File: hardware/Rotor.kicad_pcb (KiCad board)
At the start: 2 copper layers, 200 x 200 mm, 0 parts

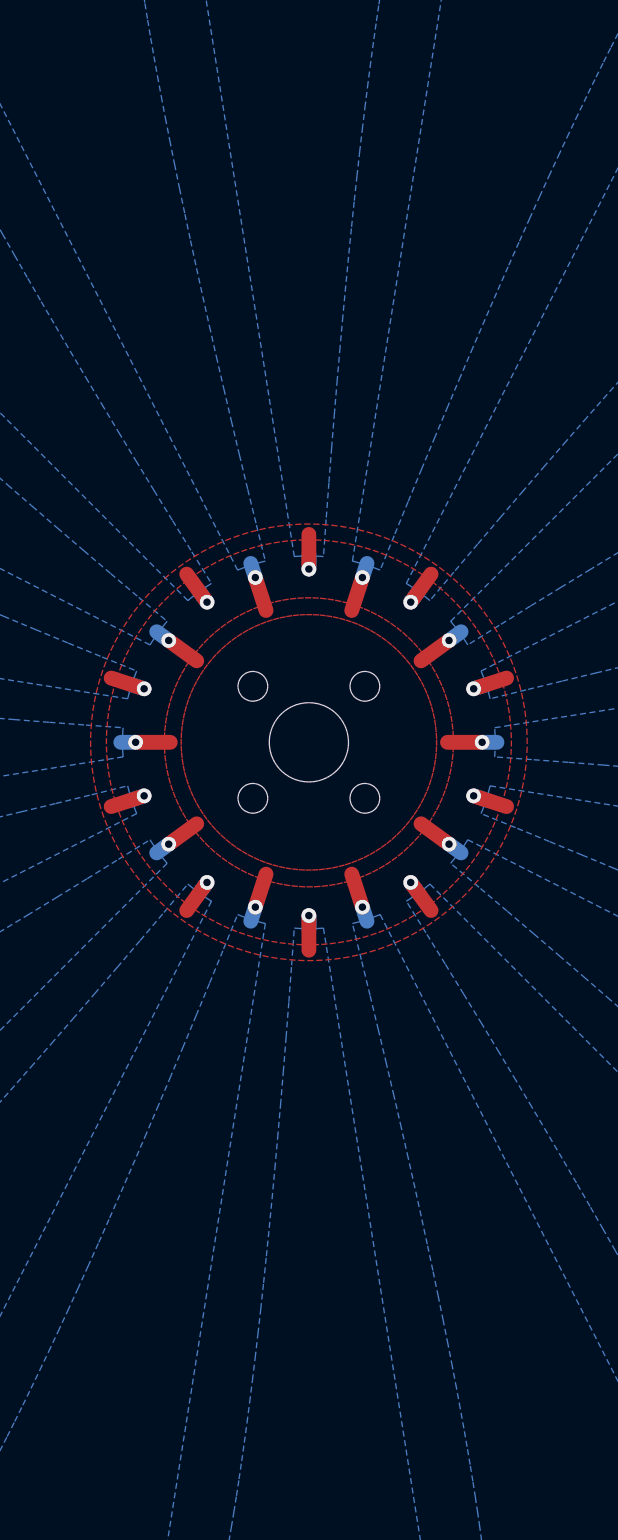
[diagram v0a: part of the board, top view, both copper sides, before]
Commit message: Libraries and generator design
Updated the generator design.
Added a libraries folder.
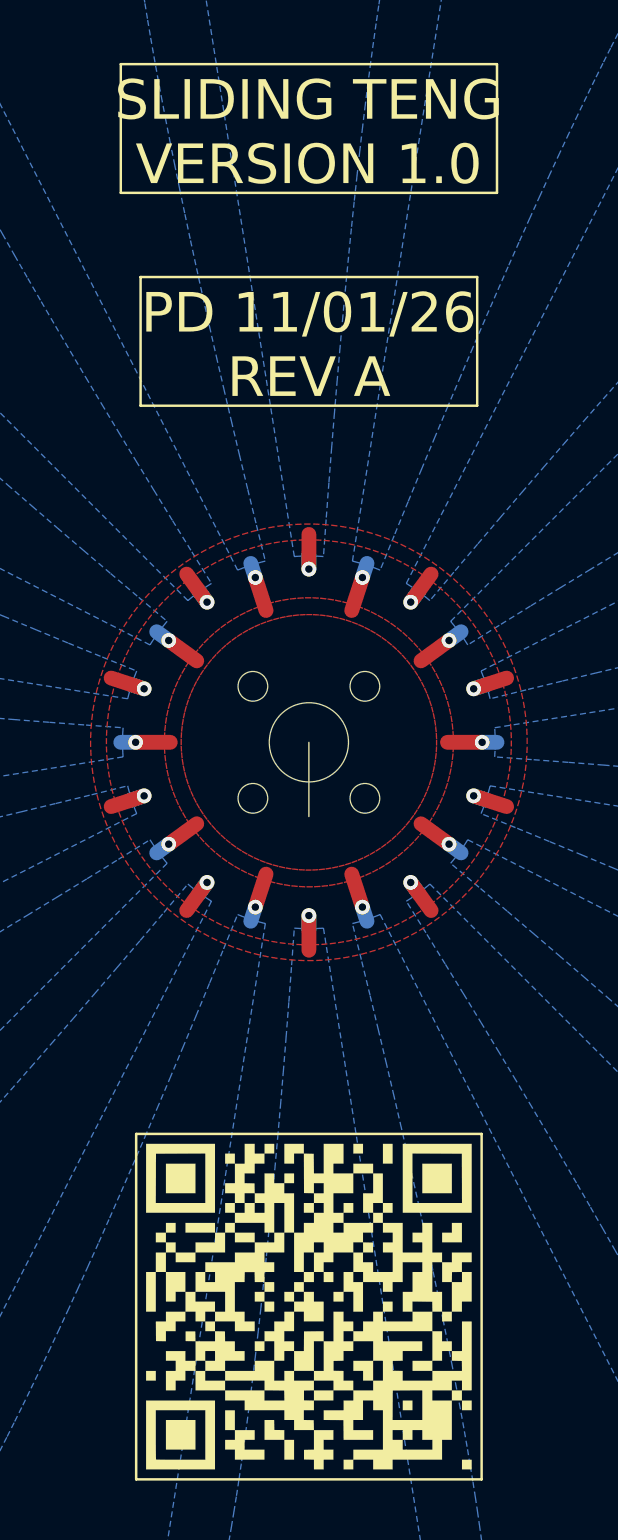
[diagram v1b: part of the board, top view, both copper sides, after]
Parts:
- added G***: LOGO, TENG:QR, F.Cu at (200.0, 207.0)
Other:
- board text added: "PD 11/01/26"
- board text added: "REV A"
- board text added: "SLIDING TENG"
- board text added: "VERSION 1.0"

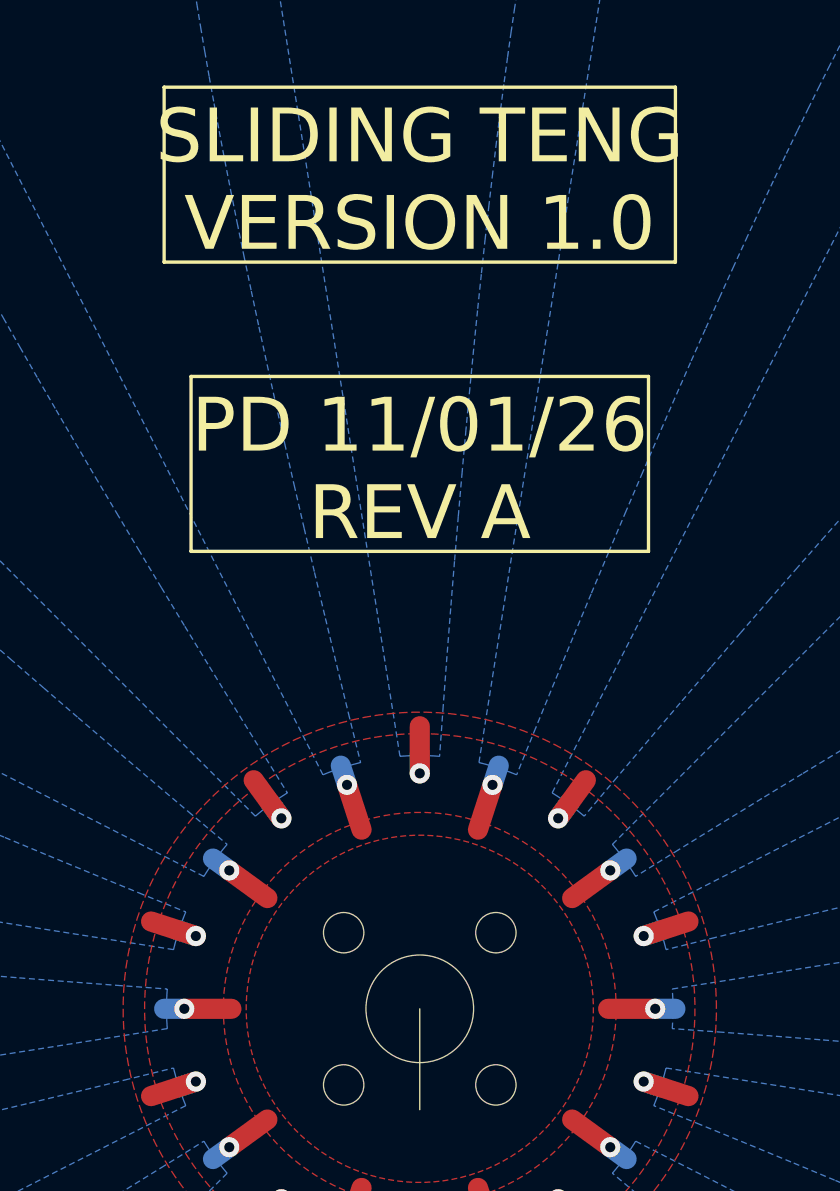
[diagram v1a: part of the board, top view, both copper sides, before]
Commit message: Generator design
Updated the rotor board design.
Updated the stator board design.
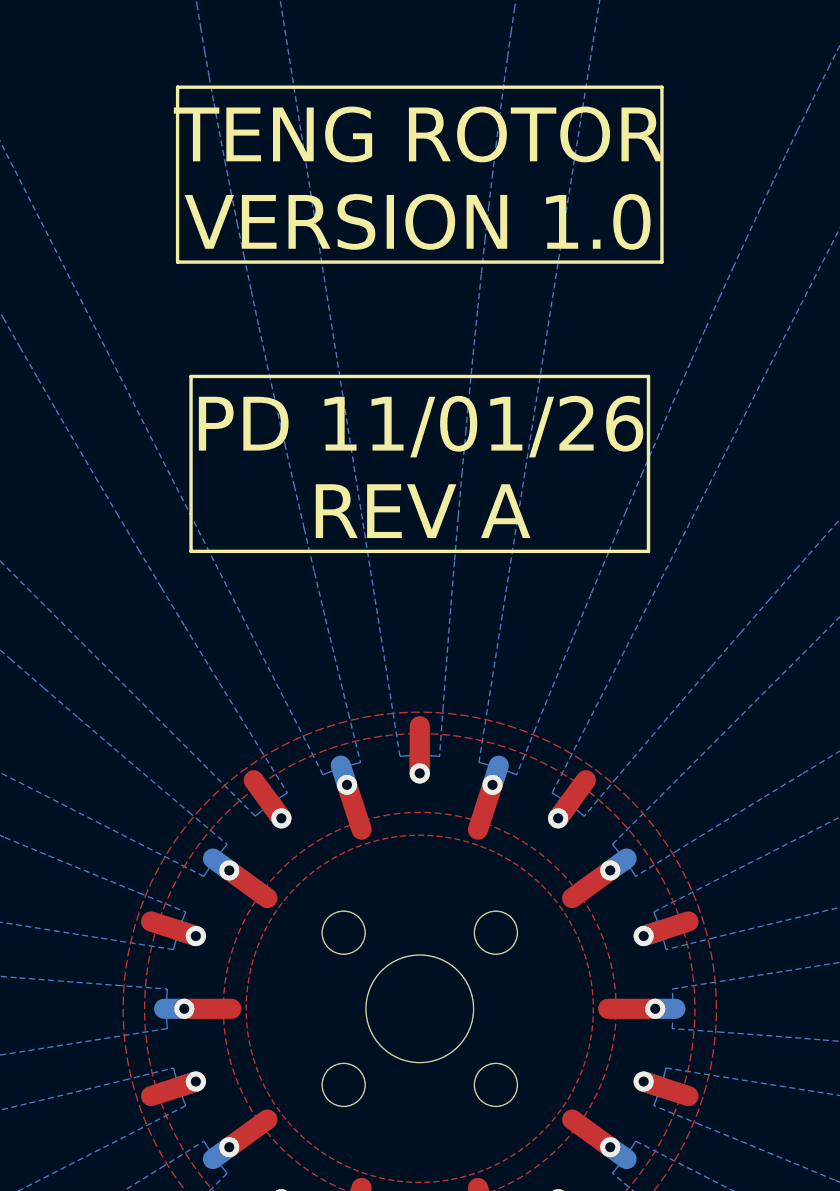
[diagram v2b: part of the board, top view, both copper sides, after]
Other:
- outline, holes or cut-outs redrawn
- board text added: "TENG ROTOR"
- board text removed: "SLIDING TENG"

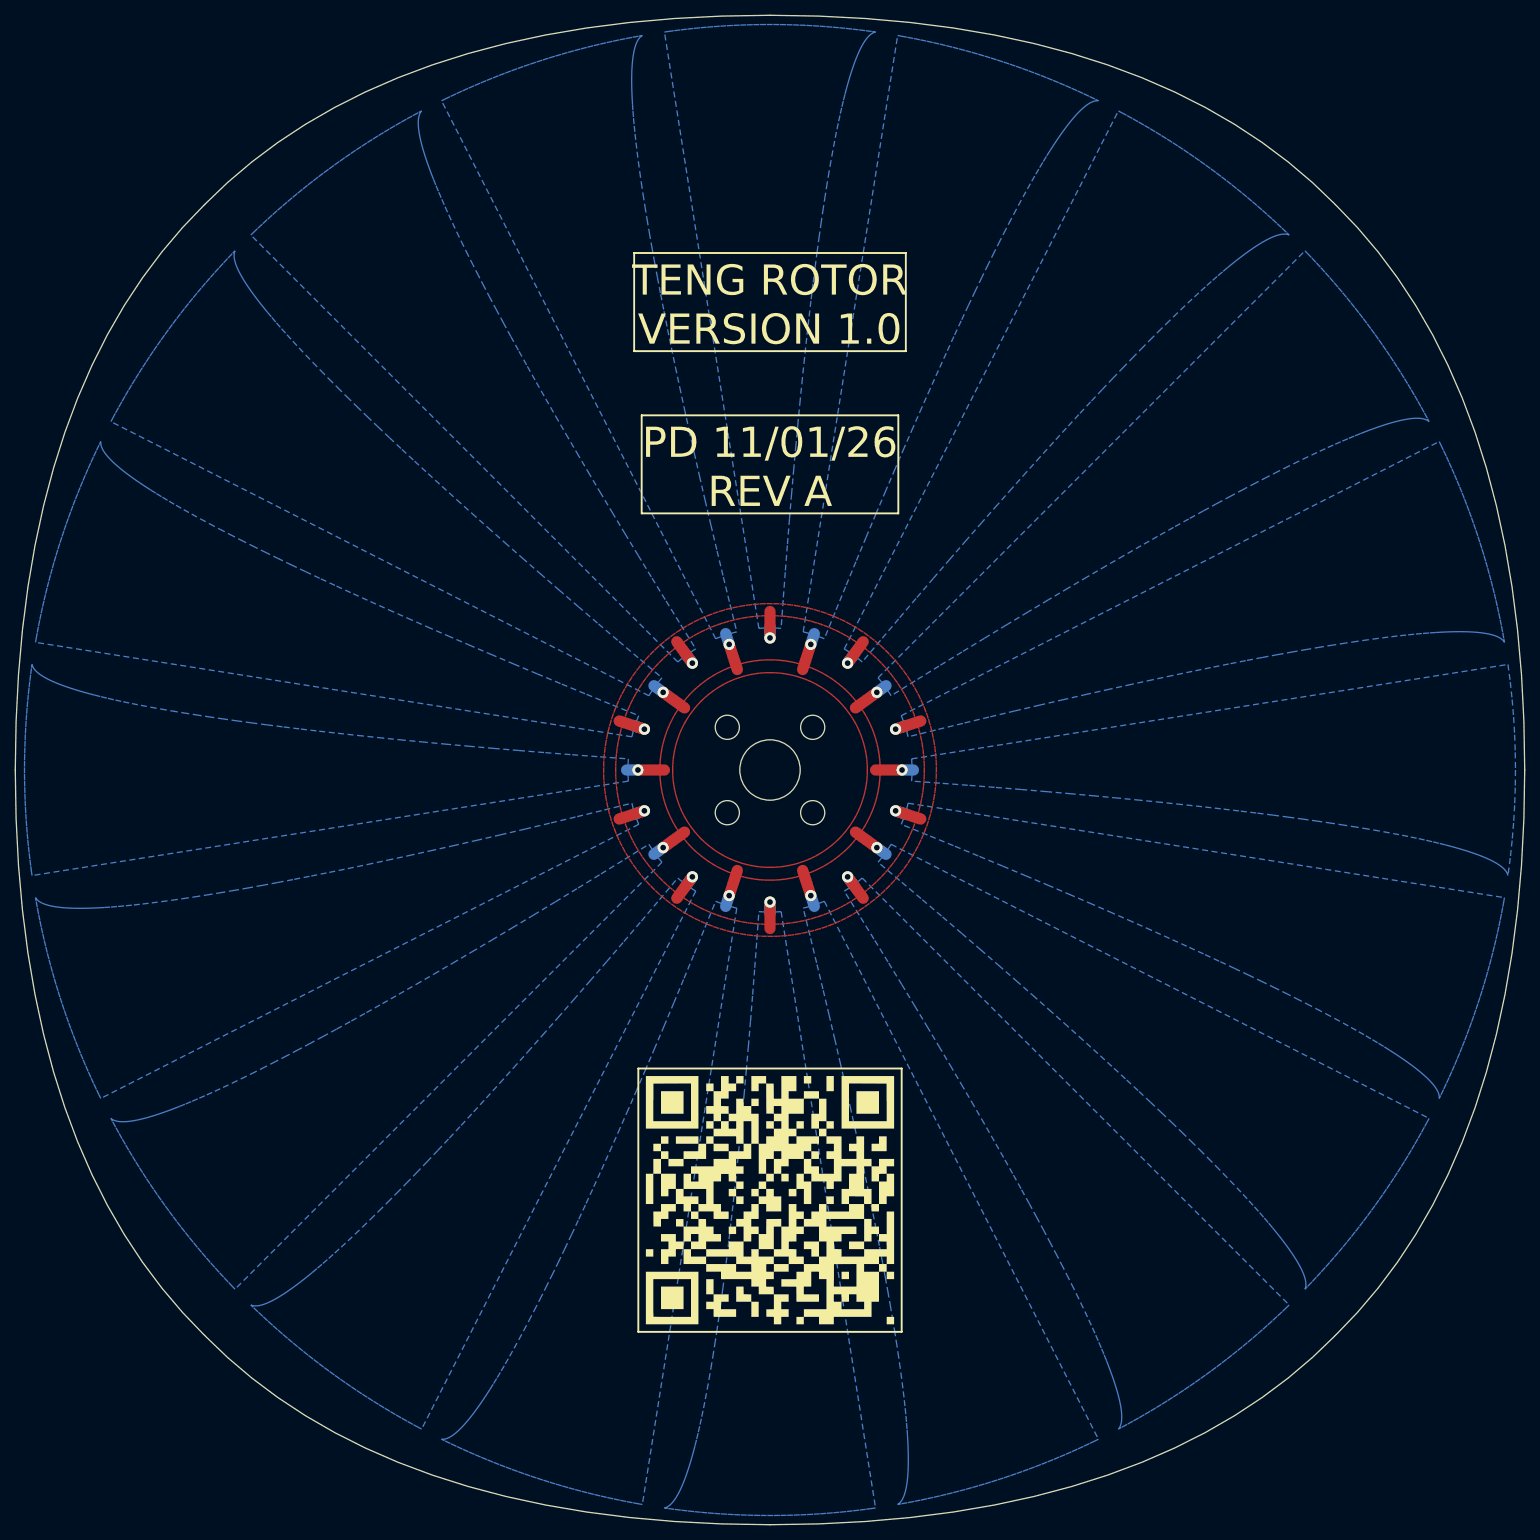
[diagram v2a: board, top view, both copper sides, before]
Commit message: Project update
Updated the project to work with KiCad 10.0.
Updated the exposed pad areas for both layouts.
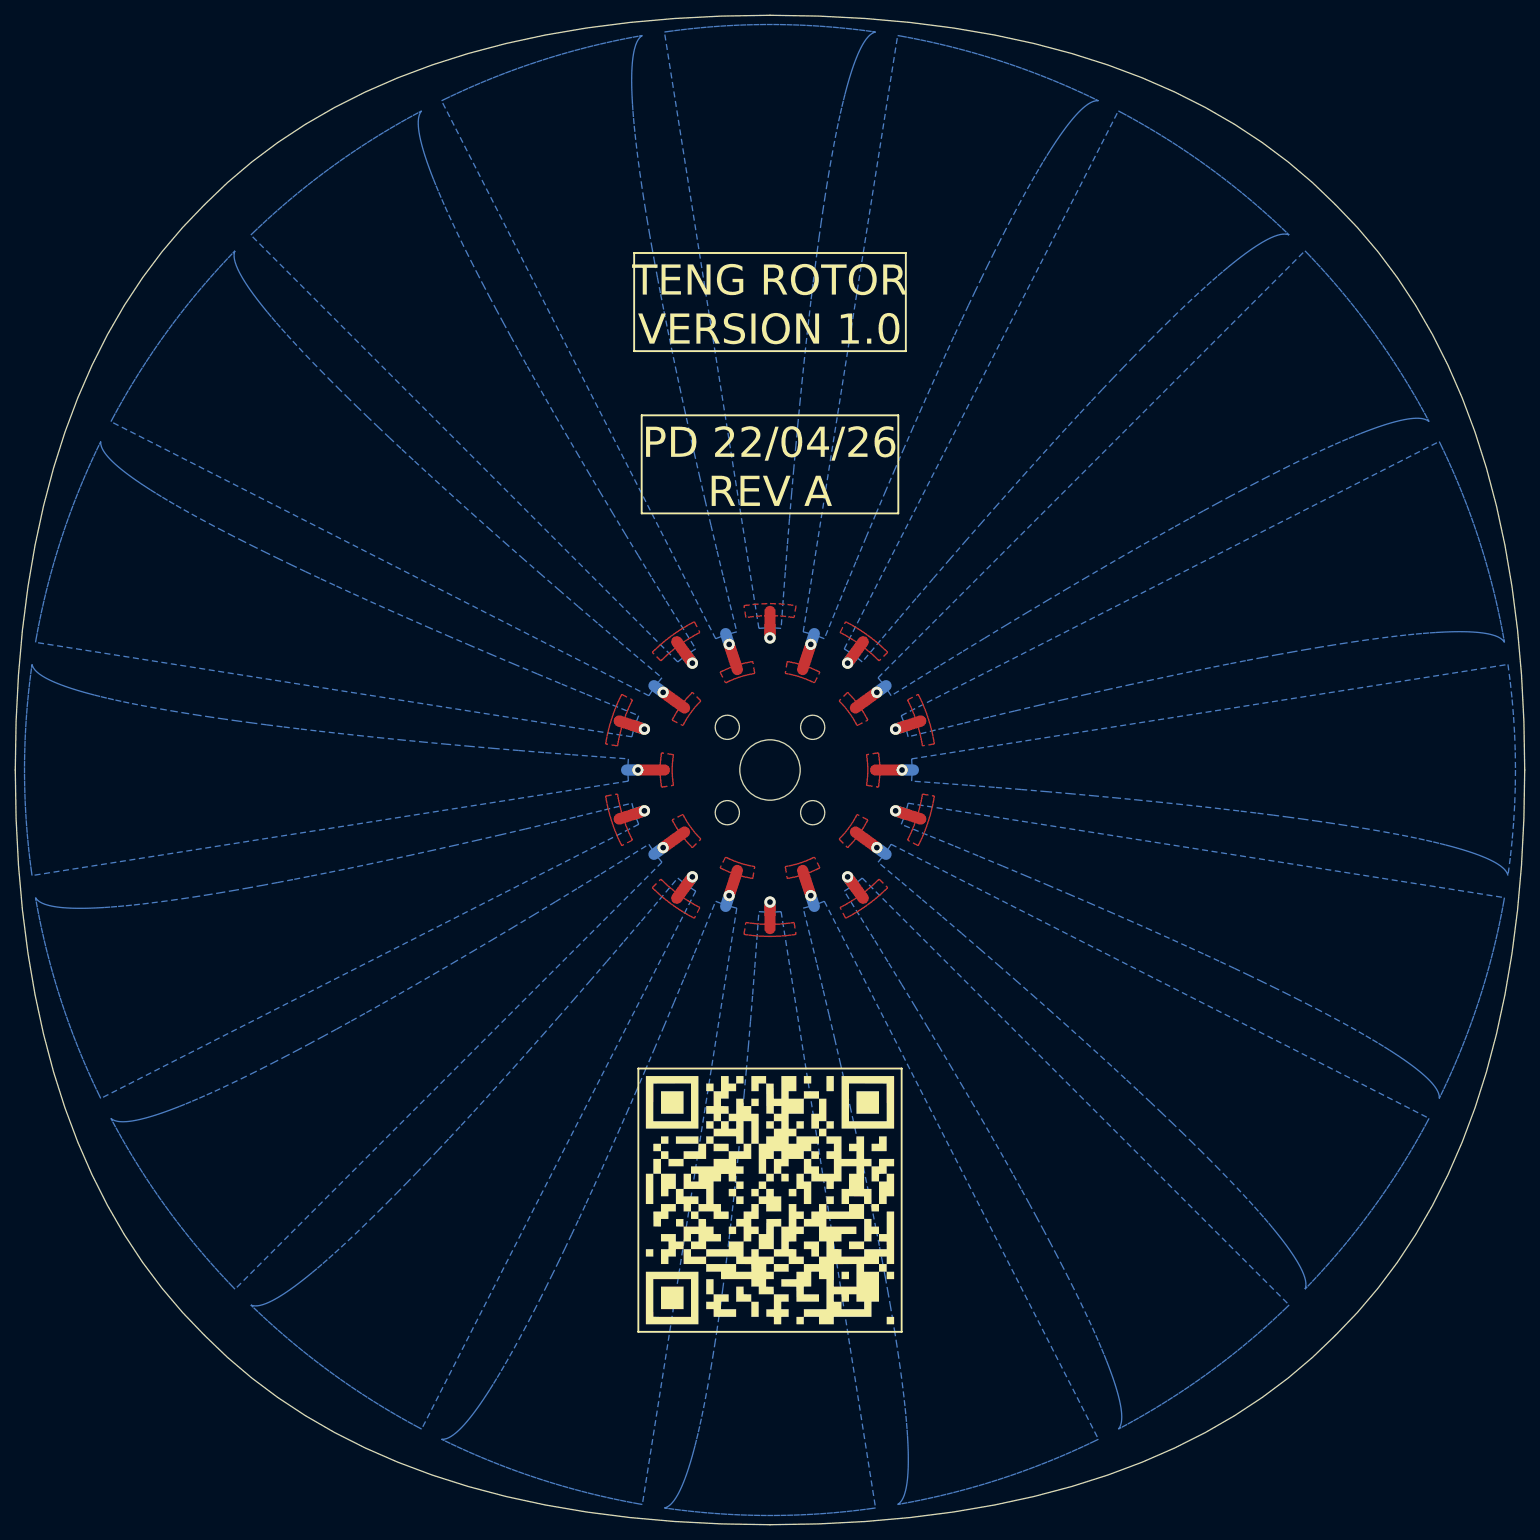
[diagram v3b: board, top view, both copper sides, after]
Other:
- board text added: "PD 22/04/26"
- board text removed: "PD 11/01/26"
